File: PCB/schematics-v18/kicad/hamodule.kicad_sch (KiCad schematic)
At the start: 94 parts, among them J1 Conn_01x02_Male, J10 2604-1104, J11 ESP Relays, J12 2604-1104, J13 EspSense, J2 2604-1102, J3 GND|5V, J4 GND|3.3V, J5 Jumper, J6 Conn_01x02_Male, J7 Current Jumper, J8 USB_C_Receptacle_USB2.0, J9 DoNotCon, K1 PCN-105D, K2 PCN-105D, K3 PCN-105D, K4 PCN-105D, Q1 SS8050-SMD, Q2 SS8050, SW1 EN, SW2 IO0, U1 LD1117AV33_TO220, U2 ESP32-WROOM-32E, U3 CP2102N-A01-GQFN28, U4 ULN2003A, U5 LDA210-PDIP, U6 LDA210-PDIP, U7 SHT4x

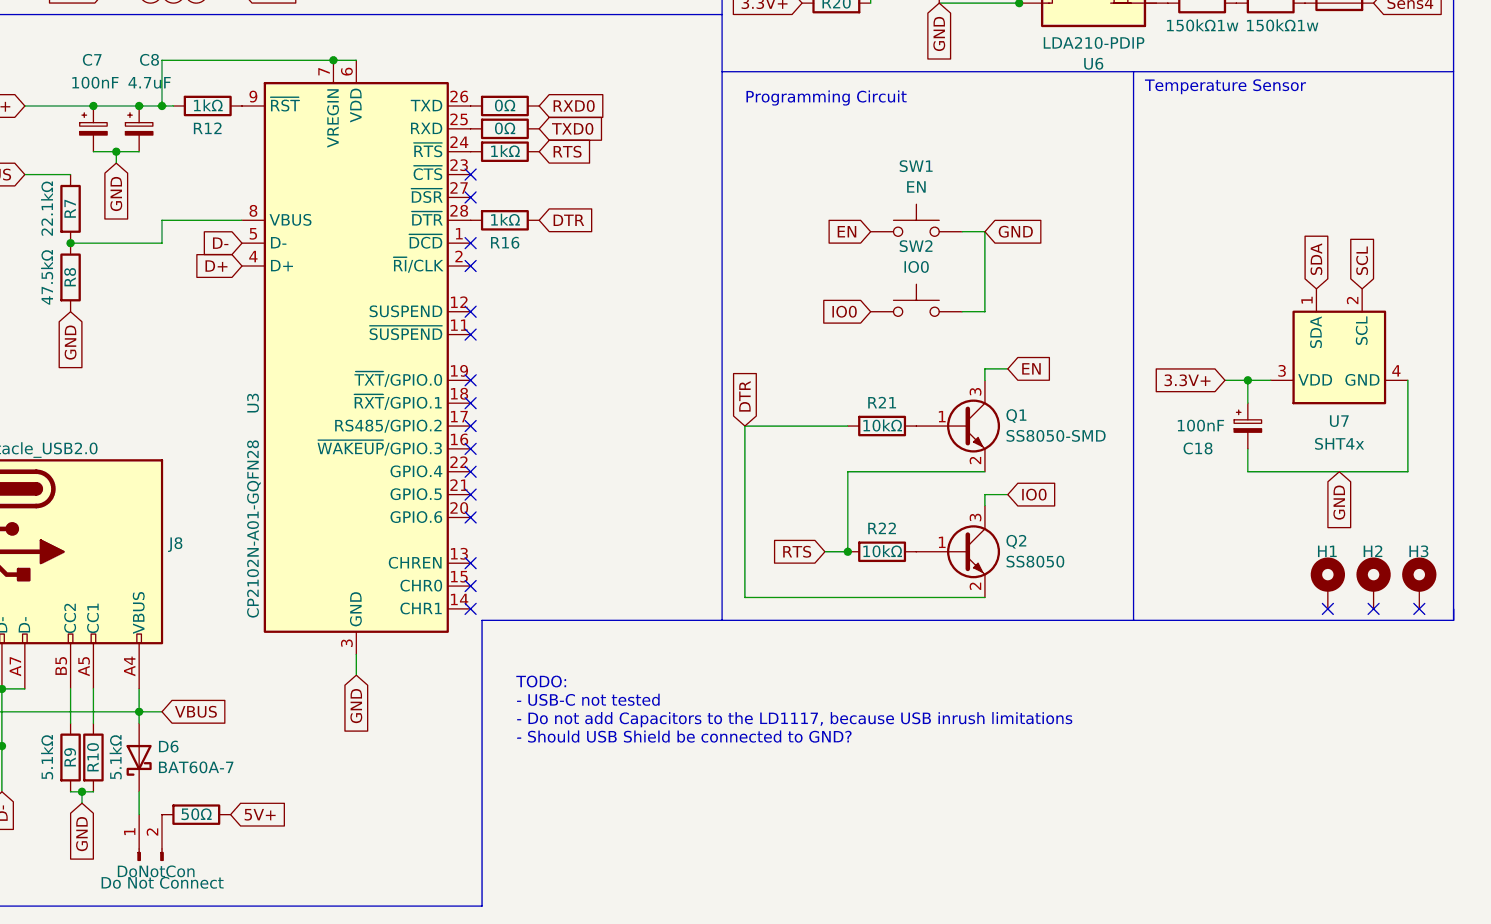
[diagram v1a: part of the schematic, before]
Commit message: removing useless USB resistor
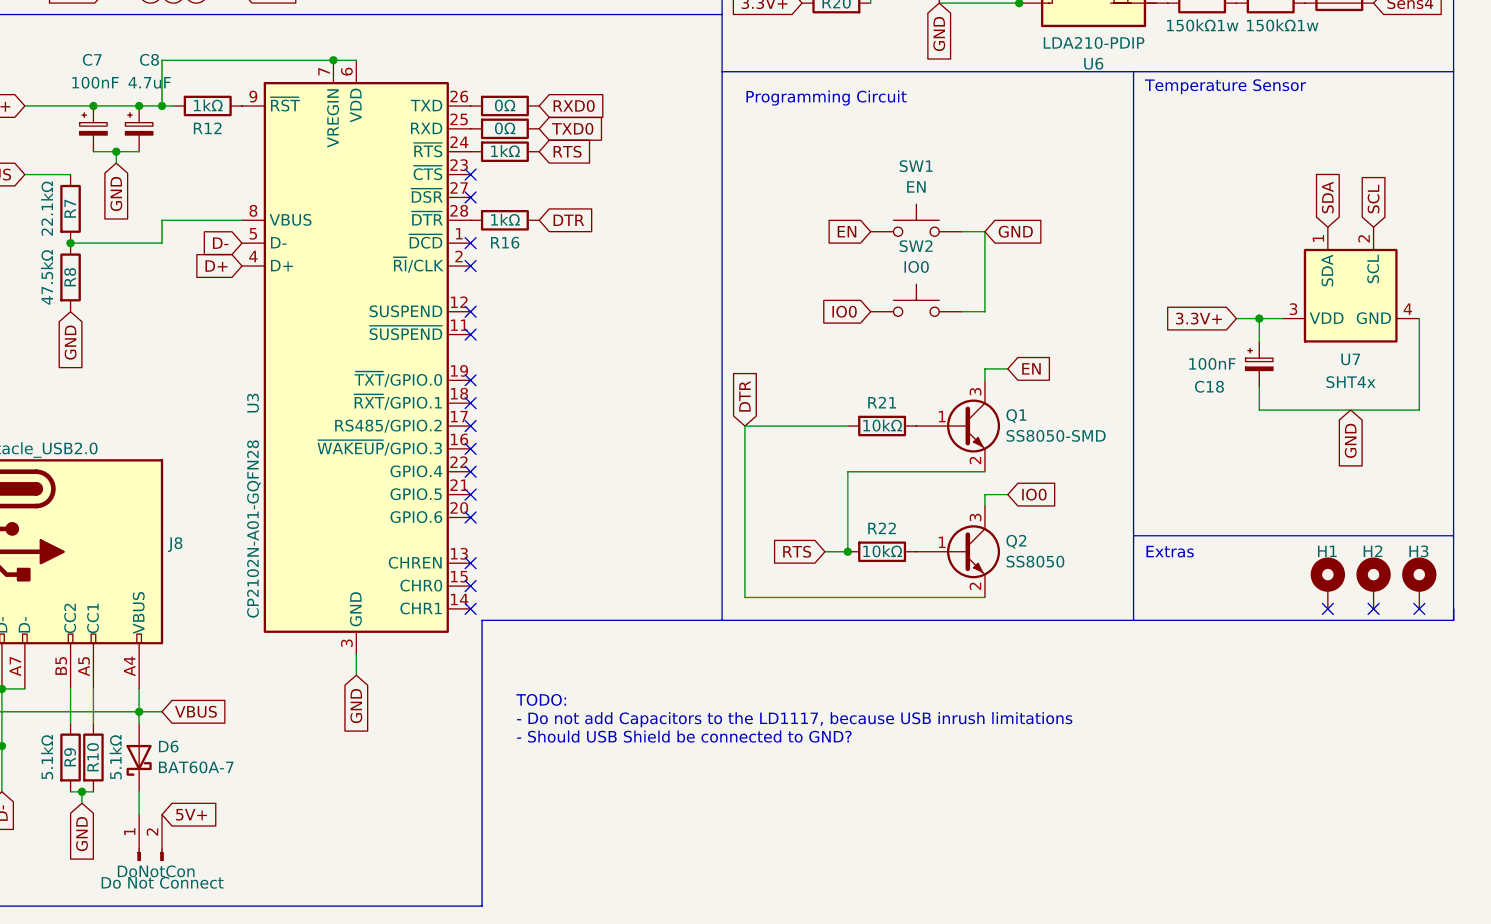
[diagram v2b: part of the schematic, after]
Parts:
- removed R11: 50Ω, Resistor_SMD:R_0805_2012Metric_Pad1.20x1.40mm_HandSolder, symbol Device:R
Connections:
- net 5V+: now also J9.2 (Pin_2)
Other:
- note added: "Extras"
- note added: "TODO: - Do not add Capacitors to the LD1117, because USB inrush limitations - Should USB Shield be connected to GND?"
- note removed: "TODO: - USB-C not tested - Do not add Capacitors to the LD1117, because USB inrush limitations - Should USB Shield be connected to GND?"
- moved on the sheet: C18, U7
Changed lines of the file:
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@@
   (junction (at 97.79 157.48) (diameter 0) (color 0 0 0 0)
   )
-  (junction (at 260.35 138.43) (diameter 0) (color 0 0 0 0)
+  (junction (at 261.62 131.572) (diameter 0) (color 0 0 0 0)
   )
   (junction (at 226.06 62.23) (diameter 0) (color 0 0 0 0)
@@
     (stroke (width 0) (type default) (color 0 0 0 0))
   )
-  (wire (pts (xy 257.81 138.43) (xy 260.35 138.43))
+  (wire (pts (xy 259.08 131.572) (xy 261.62 131.572))
     (stroke (width 0) (type default) (color 0 0 0 0))
   )
@@
     (stroke (width 0) (type default) (color 0 0 0 0))
   )
+  (polyline (pts (xy 247.65 155.702) (xy 283.21 155.702))
+    (stroke (width 0) (type default) (color 0 0 0 0))
+  )
   (wire (pts (xy 130.81 184.15) (xy 130.81 185.42))
     (stroke (width 0) (type default) (color 0 0 0 0))
@@
     (stroke (width 0) (type default) (color 0 0 0 0))
   )
-  (wire (pts (xy 260.35 146.05) (xy 260.35 148.59))
+  (wire (pts (xy 261.62 139.192) (xy 261.62 141.732))
     (stroke (width 0) (type default) (color 0 0 0 0))
   )
@@
     (stroke (width 0) (type default) (color 0 0 0 0))
   )
-  (wire (pts (xy 278.13 148.59) (xy 278.13 138.43))
+  (wire (pts (xy 279.4 141.732) (xy 279.4 131.572))
     (stroke (width 0) (type default) (color 0 0 0 0))
   )
@@
     (stroke (width 0) (type default) (color 0 0 0 0))
   )
-  (wire (pts (xy 260.35 148.59) (xy 278.13 148.59))
+  (wire (pts (xy 261.62 141.732) (xy 279.4 141.732))
     (stroke (width 0) (type default) (color 0 0 0 0))
   )
@@
     (stroke (width 0) (type default) (color 0 0 0 0))
   )
-  (wire (pts (xy 260.35 138.43) (xy 260.35 140.97))
+  (wire (pts (xy 261.62 131.572) (xy 261.62 134.112))
     (stroke (width 0) (type default) (color 0 0 0 0))
   )
@@
     (stroke (width 0) (type default) (color 0 0 0 0))
   )
-  (wire (pts (xy 260.35 138.43) (xy 262.89 138.43))
+  (wire (pts (xy 261.62 131.572) (xy 264.16 131.572))
     (stroke (width 0) (type default) (color 0 0 0 0))
   )
@@
     (effects (font (size 1.27 1.27)) (justify left bottom))
   )
+  (text "Extras" (at 248.92 158.496 0)
+    (effects (font (size 1.27 1.27)) (justify left bottom))
+  )
   (text "ESP32 WRoom" (at 72.39 101.6 0)
     (effects (font (size 1.27 1.27)) (justify left bottom))
   )
-  (text "TODO:\n- USB-C not tested\n- Do not add Capacitors to the LD1117, because USB inrush limitations\n- Should USB Shield be connected to GND?"
+  (text "TODO:\n- Do not add Capacitors to the LD1117, because USB inrush limitations\n- Should USB Shield be connected to GND?"
     (at 179.07 179.07 0)
     (effects (font (size 1.27 1.27)) (justify left bottom))
@@
     )
   )
-  (global_label "GND" (shape input) (at 270.51 148.59 270) (fields_autoplaced)
+  (global_label "GND" (shape input) (at 271.78 141.732 270) (fields_autoplaced)
     (effects (font (size 1.27 1.27)) (justify right))
-    (property "Intersheet References" "${INTERSHEET_REFS}" (id 0) (at 153.67 389.89 0)
+    (property "Intersheet References" "${INTERSHEET_REFS}" (id 0) (at 154.94 383.032 0)
       (effects (font (size 1.27 1.27)) hide)
     )
@@
     )
   )
-  (global_label "SDA" (shape input) (at 267.97 128.27 90) (fields_autoplaced)
+  (global_label "SDA" (shape input) (at 269.24 121.412 90) (fields_autoplaced)
     (effects (font (size 1.27 1.27)) (justify left))
-    (property "Intersheet References" "${INTERSHEET_REFS}" (id 0) (at 267.8906 122.3777 90)
+    (property "Intersheet References" "${INTERSHEET_REFS}" (id 0) (at 269.1606 115.5197 90)
       (effects (font (size 1.27 1.27)) (justify left) hide)
     )
@@
     )
   )
-  (global_label "3.3V+" (shape input) (at 257.81 138.43 180) (fields_autoplaced)
+  (global_label "3.3V+" (shape input) (at 259.08 131.572 180) (fields_autoplaced)
     (effects (font (size 1.27 1.27)) (justify right))
-    (property "Intersheet References" "${INTERSHEET_REFS}" (id 0) (at 143.51 384.81 0)
+    (property "Intersheet References" "${INTERSHEET_REFS}" (id 0) (at 144.78 377.952 0)
       (effects (font (size 1.27 1.27)) hide)
     )
@@
     )
   )
-  (global_label "5V+" (shape input) (at 147.32 186.69 0) (fields_autoplaced)
+  (global_label "5V+" (shape input) (at 139.7 186.69 0) (fields_autoplaced)
     (effects (font (size 1.27 1.27)) (justify left))
-    (property "Intersheet References" "${INTERSHEET_REFS}" (id 0) (at 26.67 2.54 0)
+    (property "Intersheet References" "${INTERSHEET_REFS}" (id 0) (at 19.05 2.54 0)
       (effects (font (size 1.27 1.27)) hide)
     )
@@
     )
   )
-  (global_label "SCL" (shape input) (at 273.05 128.27 90) (fields_autoplaced)
+  (global_label "SCL" (shape input) (at 274.32 121.412 90) (fields_autoplaced)
     (effects (font (size 1.27 1.27)) (justify left))
-    (property "Intersheet References" "${INTERSHEET_REFS}" (id 0) (at 272.9706 122.4382 90)
+    (property "Intersheet References" "${INTERSHEET_REFS}" (id 0) (at 274.2406 115.5802 90)
       (effects (font (size 1.27 1.27)) (justify left) hide)
     )
@@
     (pin "2")
   )
-  (symbol (lib_id "Device:C_Polarized_Small") (at 260.35 143.51 0) (unit 1)
+  (symbol (lib_id "Device:C_Polarized_Small") (at 261.62 136.652 0) (unit 1)
     (in_bom yes) (on_board yes)
-    (property "Reference" "C18" (id 0) (at 256.54 146.05 0)
+    (property "Reference" "C18" (id 0) (at 257.81 139.192 0)
       (effects (font (size 1.27 1.27)) (justify right))
     )
-    (property "Value" "100nF" (id 1) (at 257.81 143.51 0)
+    (property "Value" "100nF" (id 1) (at 259.08 136.652 0)
       (effects (font (size 1.27 1.27)) (justify right))
     )
-    (property "Footprint" "Capacitor_SMD:C_0603_1608Metric_Pad1.08x0.95mm_HandSolder" (id 2) (at 260.35 143.51 0)
+    (property "Footprint" "Capacitor_SMD:C_0603_1608Metric_Pad1.08x0.95mm_HandSolder" (id 2) (at 261.62 136.652 0)
       (effects (font (size 1.27 1.27)) hide)
     )
-    (property "Datasheet" "~" (id 3) (at 260.35 143.51 0)
+    (property "Datasheet" "~" (id 3) (at 261.62 136.652 0)
       (effects (font (size 1.27 1.27)) hide)
     )
-    (property "JLCPCB" "C14663" (id 4) (at 260.35 143.51 0)
+    (property "JLCPCB" "C14663" (id 4) (at 261.62 136.652 0)
       (effects (font (size 1.27 1.27)) hide)
     )
@@
     (pin "2")
   )
-  (symbol (lib_id "Device:R") (at 143.51 186.69 270) (unit 1)
-    (in_bom yes) (on_board yes)
-    (property "Reference" "R11" (id 0) (at 147.32 180.34 90)
-      (effects (font (size 1.27 1.27)) hide)
-    )
-    (property "Value" "50Ω" (id 1) (at 143.51 186.69 90))
-    (property "Footprint" "Resistor_SMD:R_0805_2012Metric_Pad1.20x1.40mm_HandSolder" (id 2) (at 143.51 184.912 90)
-      (effects (font (size 1.27 1.27)) hide)
-    )
-    (property "Datasheet" "https://www.distrelec.ch/en/high-power-thick-film-smd-resistor-0805-150ohm-330mw-rnd-components-rnd-155hp05w3f1500t5e/p/30111774?q=*&pos=2&origPos=1787&origPageSize=50&track=true" (id 3) (at 143.51 186.69 0)
-      (effects (font (size 1.27 1.27)) hide)
-    )
-    (property "JLCPCB" "C17738" (id 4) (at 143.51 186.69 0)
-      (effects (font (size 1.27 1.27)) hide)
-    )
-    (pin "1")
-    (pin "2")
-  )
   (symbol (lib_id "power:PWR_FLAG") (at 35.56 49.53 180) (unit 1)
     (in_bom yes) (on_board yes)
@@
     (pin "2")
   )
-  (symbol (lib_id "sht40:SHT4x") (at 270.51 135.89 90) (unit 1)
+  (symbol (lib_id "sht40:SHT4x") (at 271.78 129.032 90) (unit 1)
     (in_bom yes) (on_board yes) (fields_autoplaced)
-    (property "Reference" "U7" (id 0) (at 270.51 143.0004 90))
-    (property "Value" "SHT4x" (id 1) (at 270.51 145.5373 90))
-    (property "Footprint" "sht40:XDCR_SHT40-AD1B-R2" (id 2) (at 279.4 130.81 0)
+    (property "Reference" "U7" (id 0) (at 271.78 136.1424 90))
+    (property "Value" "SHT4x" (id 1) (at 271.78 138.6793 90))
+    (property "Footprint" "sht40:XDCR_SHT40-AD1B-R2" (id 2) (at 280.67 123.952 0)
       (effects (font (size 1.27 1.27)) hide)
     )
-    (property "Datasheet" "https://sensirion.com/media/documents/33FD6951/61641E1E/Sensirion_Humidity_Sensors_SHT4x_Datasheet.pdf" (id 3) (at 288.29 129.54 0)
+    (property "Datasheet" "https://sensirion.com/media/documents/33FD6951/61641E1E/Sensirion_Humidity_Sensors_SHT4x_Datasheet.pdf" (id 3) (at 289.56 122.682 0)
       (effects (font (size 1.27 1.27)) hide)
     )
-    (property "JLCPCB" "C2909890" (id 4) (at 270.51 135.89 0)
+    (property "JLCPCB" "C2909890" (id 4) (at 271.78 129.032 0)
       (effects (font (size 1.27 1.27)) hide)
     )
@@
       (reference "R10") (unit 1) (value "5.1kΩ") (footprint "Resistor_SMD:R_0603_1608Metric_Pad0.98x0.95mm_HandSolder")
     )
-    (path "/01368047-eec6-48b4-818c-9d56912899a3"
-      (reference "R11") (unit 1) (value "50Ω") (footprint "Resistor_SMD:R_0805_2012Metric_Pad1.20x1.40mm_HandSolder")
-    )
     (path "/00000000-0000-0000-0000-000061caa7bc"

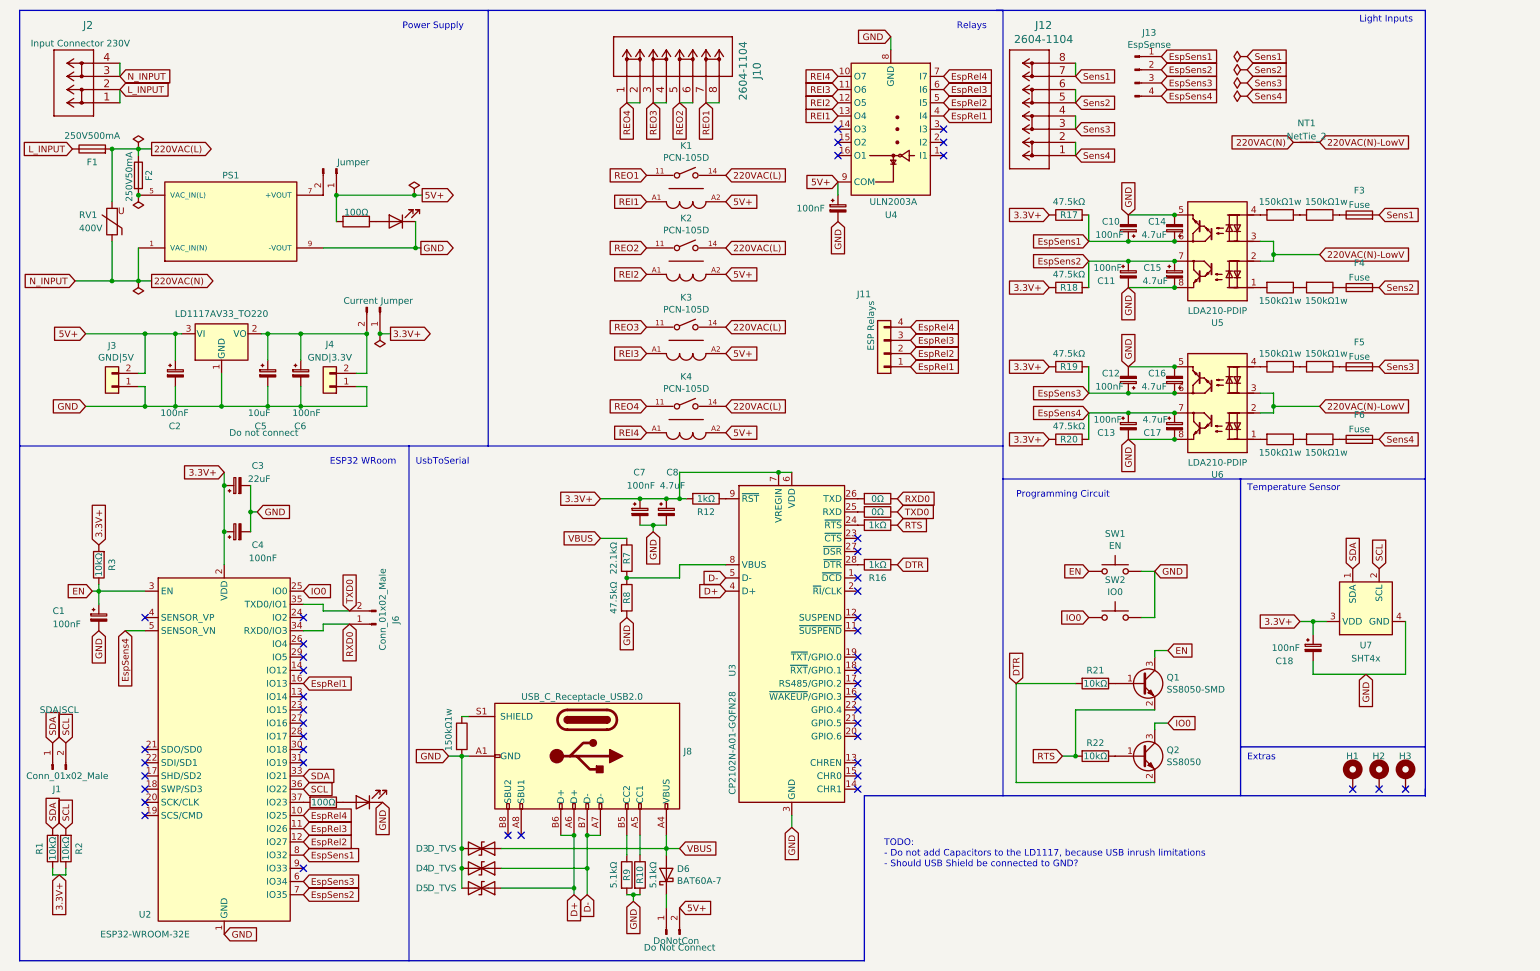
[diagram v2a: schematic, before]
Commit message: adding fuses for output + 3d modules for wago
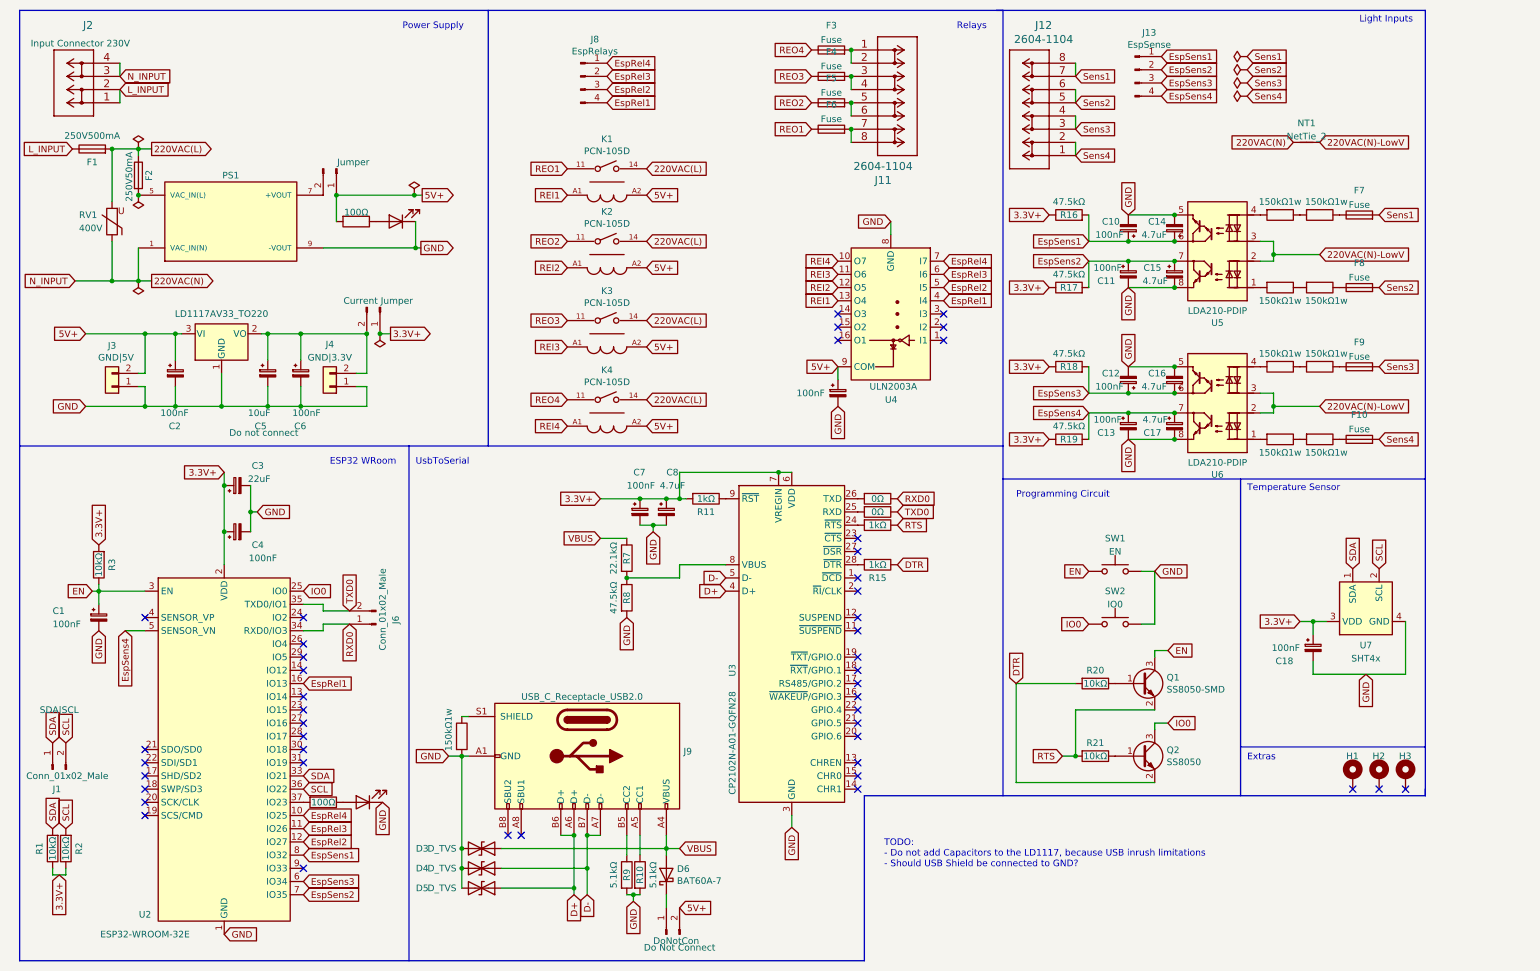
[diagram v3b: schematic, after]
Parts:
- removed J11: ESP Relays, Connector_JST:JST_XH_B4B-XH-A_1x04_P2.50mm_Vertical, symbol Connector_Generic:Conn_01x04
- added F3, F4, F5, F6: Fuse, RST-80-AMMO:FUSE_RST-1-BULK, symbol Device:Fuse
- added J8: EspRelays, Connector_PinSocket_2.54mm:PinSocket_1x04_P2.54mm_Vertical, symbol Connector:Conn_01x04_Male
- SW1: value EN -> (none); footprint Button_Switch_SMD:SW_SPST_SKQG_WithStem -> (none); Label (none) -> EN
- SW2: value IO0 -> (none); footprint Button_Switch_SMD:SW_SPST_SKQG_WithStem -> (none); Label (none) -> IO0
- renumbered F6 to F10, F3 to F7, F4 to F8, F5 to F9, J9 to J10, J10 to J11, J8 to J9, R12 to R11, R13 to R12, R14 to R13, R15 to R14, R16 to R15, R17 to R16, R18 to R17, R19 to R18, R20 to R19, R21 to R20, R22 to R21, R23 to R22, R24 to R23, R25 to R24, R26 to R25, R27 to R26, R28 to R27, R29 to R28, R30 to R29
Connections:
- net EspRel1: now also J8.4 (Pin_4)
- net EspRel2: now also J8.3 (Pin_3)
- net EspRel3: now also J8.2 (Pin_2)
- net EspRel4: now also J8.1 (Pin_1)
- net REO1: now also F6.1; no longer J11.7, J11.8
- net REO2: now also F5.1; no longer J11.5, J11.6
- net REO3: now also F4.1; no longer J11.3, J11.4
- net REO4: now also F3.1; no longer J11.1, J11.2
- new net: F3.2, J11.1, J11.2
- new net: F4.2, J11.3, J11.4
- new net: F5.2, J11.5, J11.6
- new net: F6.2, J11.7, J11.8
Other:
- moved on the sheet: J11, K1, K2, K3, K4, SW2, U4
